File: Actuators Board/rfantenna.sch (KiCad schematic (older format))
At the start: 4 parts

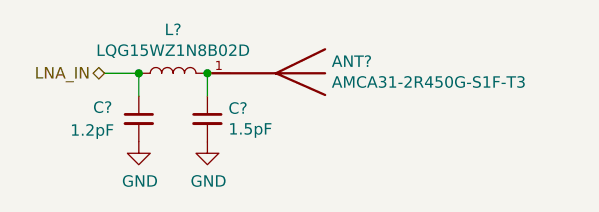
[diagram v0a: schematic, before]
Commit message: Most footprint assignments on dc motor board
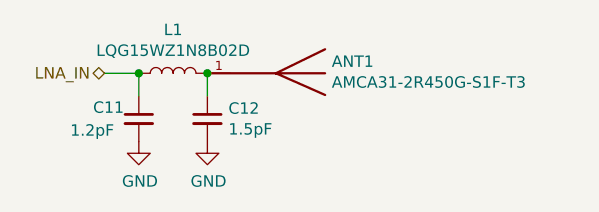
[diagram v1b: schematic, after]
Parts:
- ANT1: renamed from ANT?; footprint ANT_AMCA31-2R450G-S1F-T3 -> iclr:ANT_AMCA31-2R450G-S1F-T3
- C11, C12: renamed from C?; footprint (none) -> Capacitor_SMD:C_0603_1608Metric
- L1: renamed from L?; footprint (none) -> Inductor_SMD:L_0402_1005Metric_Pad0.77x0.64mm_HandSolder
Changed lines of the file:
@@
 $EndDescr
 $Comp
-L iclr:AMCA31-2R450G-S1F-T3 ANT?
+L iclr:AMCA31-2R450G-S1F-T3 ANT1
 U 1 1 61A4FE29
 P 6200 1650
-F 0 "ANT?" V 6149 1994 50  0000 L CNN
+F 0 "ANT1" V 6149 1994 50  0000 L CNN
 F 1 "AMCA31-2R450G-S1F-T3" V 6240 1994 50  0000 L CNN
-F 2 "ANT_AMCA31-2R450G-S1F-T3" H 6200 1650 50  0001 L BNN
+F 2 "iclr:ANT_AMCA31-2R450G-S1F-T3" H 6200 1650 50  0001 L BNN
 F 3 "" H 6200 1650 50  0001 L BNN
 F 4 "05.17.2017" H 6200 1650 50  0001 L BNN "PARTREV"
@@
 $EndComp
 $Comp
-L Device:L L?
+L Device:L L1
 U 1 1 61A4FE2F
 P 5850 1650
-F 0 "L?" V 6040 1650 50  0000 C CNN
+F 0 "L1" V 6040 1650 50  0000 C CNN
 F 1 "LQG15WZ1N8B02D" V 5949 1650 50  0000 C CNN
-F 2 "" H 5850 1650 50  0001 C CNN
+F 2 "Inductor_SMD:L_0402_1005Metric_Pad0.77x0.64mm_HandSolder" H 5850 1650 50  0001 C CNN
 F 3 "~" H 5850 1650 50  0001 C CNN
 	1    5850 1650
@@
 	6000 1650 6000 1750
 $Comp
-L Device:C_Small C?
+L Device:C_Small C12
 U 1 1 61A4FE36
 P 6000 1850
-F 0 "C?" H 6092 1896 50  0000 L CNN
+F 0 "C12" H 6092 1896 50  0000 L CNN
 F 1 "1.5pF" H 6092 1805 50  0000 L CNN
-F 2 "" H 6000 1850 50  0001 C CNN
+F 2 "Capacitor_SMD:C_0603_1608Metric" H 6000 1850 50  0001 C CNN
 F 3 "~" H 6000 1850 50  0001 C CNN
 	1    6000 1850
@@
 $EndComp
 $Comp
-L power:GND #PWR?
+L power:GND #PWR0132
 U 1 1 61A4FE3C
 P 6000 1950
-F 0 "#PWR?" H 6000 1700 50  0001 C CNN
+F 0 "#PWR0132" H 6000 1700 50  0001 C CNN
 F 1 "GND" H 6005 1777 50  0000 C CNN
 F 2 "" H 6000 1950 50  0001 C CNN
@@
 Connection ~ 6000 1650
 $Comp
-L Device:C_Small C?
+L Device:C_Small C11
 U 1 1 61A4FE43
 P 5700 1850
-F 0 "C?" H 5500 1900 50  0000 L CNN
+F 0 "C11" H 5500 1900 50  0000 L CNN
 F 1 "1.2pF" H 5400 1800 50  0000 L CNN
-F 2 "" H 5700 1850 50  0001 C CNN
+F 2 "Capacitor_SMD:C_0603_1608Metric" H 5700 1850 50  0001 C CNN
 F 3 "~" H 5700 1850 50  0001 C CNN
 	1    5700 1850
@@
 	5700 1650 5700 1750
 $Comp
-L power:GND #PWR?
+L power:GND #PWR0133
 U 1 1 61A4FE4A
 P 5700 1950
-F 0 "#PWR?" H 5700 1700 50  0001 C CNN
+F 0 "#PWR0133" H 5700 1700 50  0001 C CNN
 F 1 "GND" H 5705 1777 50  0000 C CNN
 F 2 "" H 5700 1950 50  0001 C CNN
